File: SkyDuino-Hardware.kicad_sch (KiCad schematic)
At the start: 44 parts, among them J1 PWR, J10 AUX2, J2 BT, J3 ET, J4 Drum, J5 Filter, J6 Exhaust, J7 Cooling, J8 NTC, J9 AUX1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

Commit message: Add Quick Connect Tabs and footprints
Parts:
- ACL1, ACN1, HEAT1, HEAT2: value Spade Conn -> QC 19705-4303; footprint (none) -> Connectors:QuickConnect_Tab_Molex_19705-4303; Mouser pn (none) -> 538-19705-4303
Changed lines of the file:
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@@
 	)
 	(symbol
+		(lib_id "Connector_Generic:Conn_01x01")
+		(at 27.94 181.61 180)
+		(unit 1)
+		(exclude_from_sim no)
+		(in_bom yes)
+		(on_board yes)
+		(dnp no)
+		(property "Reference" "ACN1"
+			(at 22.86 181.61 0)
+			(effects
+				(font
+					(size 1.27 1.27)
+				)
+			)
+		)
+		(property "Value" "QC 19705-4303"
+			(at 27.94 177.8 0)
+			(effects
+				(font
+					(size 1.27 1.27)
+				)
+				(hide yes)
+			)
+		)
+		(property "Footprint" "Connectors:QuickConnect_Tab_Molex_19705-4303"
+			(at 27.94 181.61 0)
+			(effects
+				(font
+					(size 1.27 1.27)
+				)
+				(hide yes)
+			)
+		)
+		(property "Datasheet" "https://www.molex.com/content/dam/molex/molex-dot-com/products/automated/en-us/salesdrawingpdf/197/19705/197054303_sd.pdf"
+			(at 27.94 181.61 0)
+			(effects
+				(font
+					(size 1.27 1.27)
+				)
+				(hide yes)
+			)
+		)
+		(property "Description" "Terminals QUICK DISCONNECT TAB"
+			(at 27.94 181.61 0)
+			(effects
+				(font
+					(size 1.27 1.27)
+				)
+				(hide yes)
+			)
+		)
+		(property "Mouser pn" "538-19705-4303"
+			(at 27.94 181.61 0)
+			(effects
+				(font
+					(size 1.27 1.27)
+				)
+				(hide yes)
+			)
+		)
+		(pin "1"
+		)
+		(instances
+			(project "SkyDuino-Hardware"
+				(path "/a6671232-96de-4e23-ad68-f9378c1c0159"
+					(reference "ACN1")
+					(unit 1)
+				)
+			)
+		)
+	)
+	(symbol
 		(lib_id "power:GND")
 		(at 110.49 52.07 0)
@@
 			)
 		)
-		(property "Value" "Spade Conn"
+		(property "Value" "QC 19705-4303"
 			(at 27.94 172.72 0)
 			(effects
@@
 			)
 		)
-		(property "Footprint" ""
+		(property "Footprint" "Connectors:QuickConnect_Tab_Molex_19705-4303"
 			(at 27.94 176.53 0)
 			(effects
@@
 			)
 		)
-		(property "Datasheet" "~"
+		(property "Datasheet" "https://www.molex.com/content/dam/molex/molex-dot-com/products/automated/en-us/salesdrawingpdf/197/19705/197054303_sd.pdf"
 			(at 27.94 176.53 0)
 			(effects
@@
 			)
 		)
-		(property "Description" ""
+		(property "Description" "Terminals QUICK DISCONNECT TAB"
+			(at 27.94 176.53 0)
+			(effects
+				(font
+					(size 1.27 1.27)
+				)
+				(hide yes)
+			)
+		)
+		(property "Mouser pn" "538-19705-4303"
 			(at 27.94 176.53 0)
 			(effects
@@
 			)
 		)
-		(property "Value" "Spade Conn"
+		(property "Value" "QC 19705-4303"
 			(at 27.94 167.64 0)
 			(effects
@@
 			)
 		)
-		(property "Footprint" ""
+		(property "Footprint" "Connectors:QuickConnect_Tab_Molex_19705-4303"
 			(at 27.94 171.45 0)
 			(effects
@@
 			)
 		)
-		(property "Datasheet" "~"
+		(property "Datasheet" "https://www.molex.com/content/dam/molex/molex-dot-com/products/automated/en-us/salesdrawingpdf/197/19705/197054303_sd.pdf"
+			(at 27.94 171.45 0)
+			(effects
+				(font
+					(size 1.27 1.27)
+				)
+				(hide yes)
+			)
+		)
+		(property "Description" "Terminals QUICK DISCONNECT TAB"
 			(at 27.94 171.45 0)
 			(effects
@@
 			)
 		)
-		(property "Description" ""
+		(property "Mouser pn" "538-19705-4303"
 			(at 27.94 171.45 0)
 			(effects
@@
 	)
 	(symbol
-		(lib_id "Connector_Generic:Conn_01x01")
-		(at 27.94 186.69 180)
-		(unit 1)
-		(exclude_from_sim no)
-		(in_bom yes)
-		(on_board yes)
-		(dnp no)
-		(property "Reference" "HEAT2"
-			(at 22.86 186.69 0)
-			(effects
-				(font
-					(size 1.27 1.27)
-				)
-			)
-		)
-		(property "Value" "Spade Conn"
-			(at 20.32 186.69 0)
-			(effects
-				(font
-					(size 1.27 1.27)
-				)
-				(hide yes)
-			)
-		)
-		(property "Footprint" ""
-			(at 27.94 186.69 0)
-			(effects
-				(font
-					(size 1.27 1.27)
-				)
-				(hide yes)
-			)
-		)
-		(property "Datasheet" "~"
-			(at 27.94 186.69 0)
-			(effects
-				(font
-					(size 1.27 1.27)
-				)
-				(hide yes)
-			)
-		)
-		(property "Description" ""
-			(at 27.94 186.69 0)
-			(effects
-				(font
-					(size 1.27 1.27)
-				)
-				(hide yes)
-			)
-		)
-		(pin "1"
-		)
-		(instances
-			(project "SkyDuino-Hardware"
-				(path "/a6671232-96de-4e23-ad68-f9378c1c0159"
-					(reference "HEAT2")
-					(unit 1)
-				)
-			)
-		)
-	)
-	(symbol
 		(lib_id "Device:C")
 		(at 110.49 41.91 0)
@@
 	)
 	(symbol
-		(lib_id "Connector_Generic:Conn_01x01")
-		(at 27.94 181.61 180)
-		(unit 1)
-		(exclude_from_sim no)
-		(in_bom yes)
-		(on_board yes)
-		(dnp no)
-		(property "Reference" "ACN1"
-			(at 22.86 181.61 0)
-			(effects
-				(font
-					(size 1.27 1.27)
-				)
-			)
-		)
-		(property "Value" "Spade Conn"
-			(at 27.94 177.8 0)
-			(effects
-				(font
-					(size 1.27 1.27)
-				)
-				(hide yes)
-			)
-		)
-		(property "Footprint" ""
-			(at 27.94 181.61 0)
-			(effects
-				(font
-					(size 1.27 1.27)
-				)
-				(hide yes)
-			)
-		)
-		(property "Datasheet" "~"
-			(at 27.94 181.61 0)
-			(effects
-				(font
-					(size 1.27 1.27)
-				)
-				(hide yes)
-			)
-		)
-		(property "Description" ""
-			(at 27.94 181.61 0)
-			(effects
-				(font
-					(size 1.27 1.27)
-				)
-				(hide yes)
-			)
-		)
-		(pin "1"
-		)
-		(instances
-			(project "SkyDuino-Hardware"
-				(path "/a6671232-96de-4e23-ad68-f9378c1c0159"
-					(reference "ACN1")
-					(unit 1)
-				)
-			)
-		)
-	)
-	(symbol
 		(lib_id "Device:C_Polarized_Small")
 		(at 121.92 41.91 0)
@@
 					(unit 1)
 				)
+			)
+		)
+	)
+	(symbol
+		(lib_id "Connector_Generic:Conn_01x01")
+		(at 27.94 186.69 180)
+		(unit 1)
+		(exclude_from_sim no)
+		(in_bom yes)
+		(on_board yes)
+		(dnp no)
+		(property "Reference" "HEAT2"
+			(at 22.86 186.69 0)
+			(effects
+				(font
+					(size 1.27 1.27)
+				)
+			)
+		)
+		(property "Value" "QC 19705-4303"
+			(at 27.94 182.88 0)
+			(effects
+				(font
+					(size 1.27 1.27)
+				)
+				(hide yes)
+			)
+		)
+		(property "Footprint" "Connectors:QuickConnect_Tab_Molex_19705-4303"
+			(at 27.94 186.69 0)
+			(effects
+				(font
+					(size 1.27 1.27)
+				)
+				(hide yes)
+			)
+		)
+		(property "Datasheet" "https://www.molex.com/content/dam/molex/molex-dot-com/products/automated/en-us/salesdrawingpdf/197/19705/197054303_sd.pdf"
+			(at 27.94 186.69 0)
+			(effects
+				(font
+					(size 1.27 1.27)
+				)
+				(hide yes)
+			)
+		)
+		(property "Description" "Terminals QUICK DISCONNECT TAB"
+			(at 27.94 186.69 0)
+			(effects
+				(font
+					(size 1.27 1.27)
+				)
+				(hide yes)
+			)
+		)
+		(property "Mouser pn" "538-19705-4303"
+			(at 27.94 186.69 0)
+			(effects
+				(font
+					(size 1.27 1.27)
+				)
+				(hide yes)
+			)
+		)
+		(pin "1"
+		)
+		(instances
+			(project "SkyDuino-Hardware"
+				(path "/a6671232-96de-4e23-ad68-f9378c1c0159"
+					(reference "HEAT2")
+					(unit 1)
+				)

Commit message: Update footprints
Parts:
- J2, J3: footprint Connector_SH:KF7.62_2P -> Connectors:KF7.62_2P
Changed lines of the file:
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@@
 			)
 		)
-		(property "Footprint" "Connector_SH:KF7.62_2P"
+		(property "Footprint" "Connectors:KF7.62_2P"
 			(at 212.09 76.2 0)
 			(effects
@@
 			)
 		)
-		(property "Footprint" "Connector_SH:KF7.62_2P"
+		(property "Footprint" "Connectors:KF7.62_2P"
 			(at 212.09 38.1 0)
 			(effects

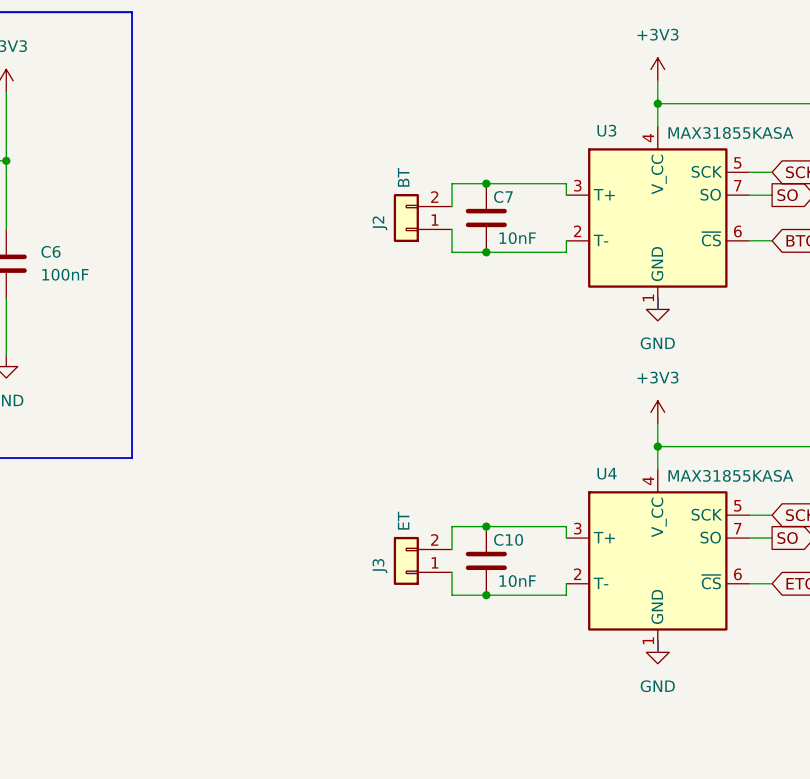
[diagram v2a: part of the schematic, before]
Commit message: Optimize pinouts
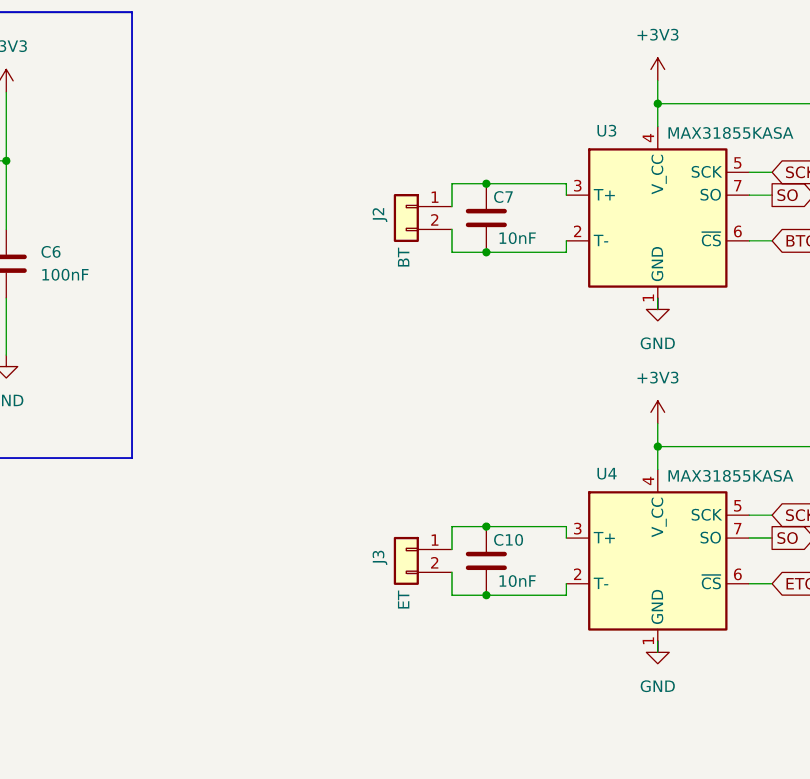
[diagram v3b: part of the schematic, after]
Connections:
- net at C10.1, U4.3 (T+): now also J3.1 (Pin_1); no longer J3.2 (Pin_2)
- net at C10.2, U4.2 (T-): now also J3.2 (Pin_2); no longer J3.1 (Pin_1)
- net at C7.1, U3.3 (T+): now also J2.1 (Pin_1); no longer J2.2 (Pin_2)
- net at C7.2, U3.2 (T-): now also J2.2 (Pin_2); no longer J2.1 (Pin_1)
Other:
- moved on the sheet: J2, J3
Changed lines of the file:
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@@
 	(symbol
 		(lib_id "Connector_Generic:Conn_01x02")
-		(at 212.09 76.2 180)
+		(at 212.09 73.66 0)
+		(mirror y)
 		(unit 1)
 		(exclude_from_sim no)
@@
 		(dnp no)
 		(property "Reference" "J3"
-			(at 209.042 76.2 90)
+			(at 209.042 73.66 90)
 			(effects
 				(font
@@
 		)
 		(property "Value" "ET"
-			(at 211.836 71.628 90)
+			(at 211.836 78.232 90)
 			(effects
 				(font
@@
 		)
 		(property "Footprint" "Connectors:KF7.62_2P"
-			(at 212.09 76.2 0)
+			(at 212.09 73.66 0)
 			(effects
 				(font
@@
 		)
 		(property "Datasheet" "~"
-			(at 212.09 76.2 0)
+			(at 212.09 73.66 0)
 			(effects
 				(font
@@
 		)
 		(property "Description" "Generic connector, single row, 01x02, script generated (kicad-library-utils/schlib/autogen/connector/)"
-			(at 212.09 76.2 0)
+			(at 212.09 73.66 0)
 			(effects
 				(font
@@
 	(symbol
 		(lib_id "Connector_Generic:Conn_01x02")
-		(at 212.09 38.1 180)
+		(at 212.09 35.56 0)
+		(mirror y)
 		(unit 1)
 		(exclude_from_sim no)
@@
 		(dnp no)
 		(property "Reference" "J2"
-			(at 209.042 38.1 90)
+			(at 209.042 35.56 90)
 			(effects
 				(font
@@
 		)
 		(property "Value" "BT"
-			(at 211.836 33.528 90)
+			(at 211.836 40.132 90)
 			(effects
 				(font
@@
 		)
 		(property "Footprint" "Connectors:KF7.62_2P"
-			(at 212.09 38.1 0)
+			(at 212.09 35.56 0)
 			(effects
 				(font
@@
 		)
 		(property "Datasheet" "~"
-			(at 212.09 38.1 0)
+			(at 212.09 35.56 0)
 			(effects
 				(font
@@
 		)
 		(property "Description" "Generic connector, single row, 01x02, script generated (kicad-library-utils/schlib/autogen/connector/)"
-			(at 212.09 38.1 0)
+			(at 212.09 35.56 0)
 			(effects
 				(font

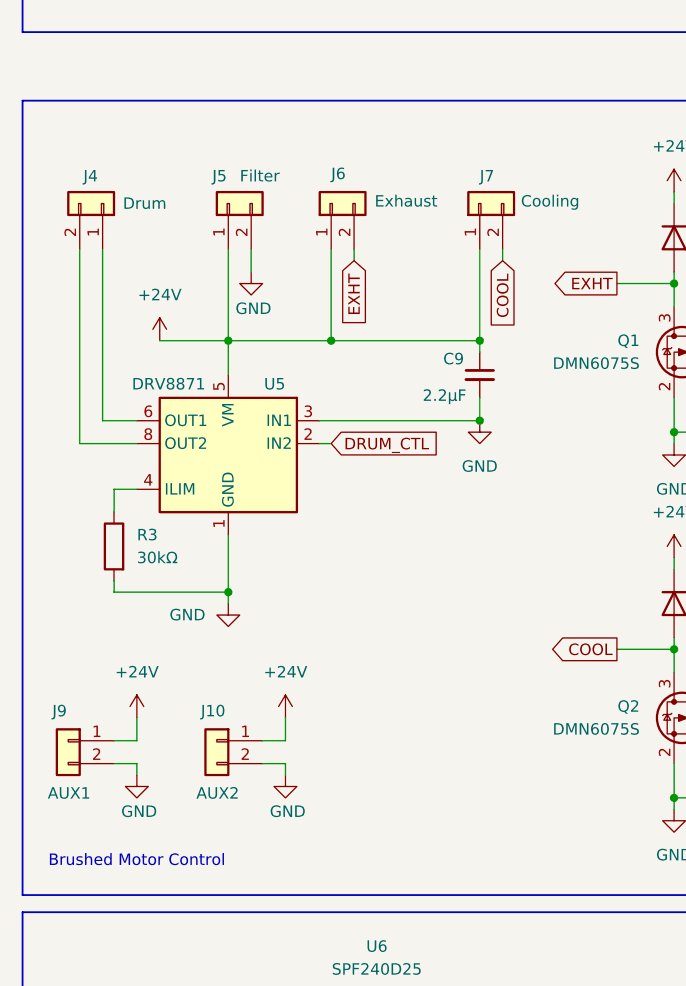
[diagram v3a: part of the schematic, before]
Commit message: Optimize pinouts
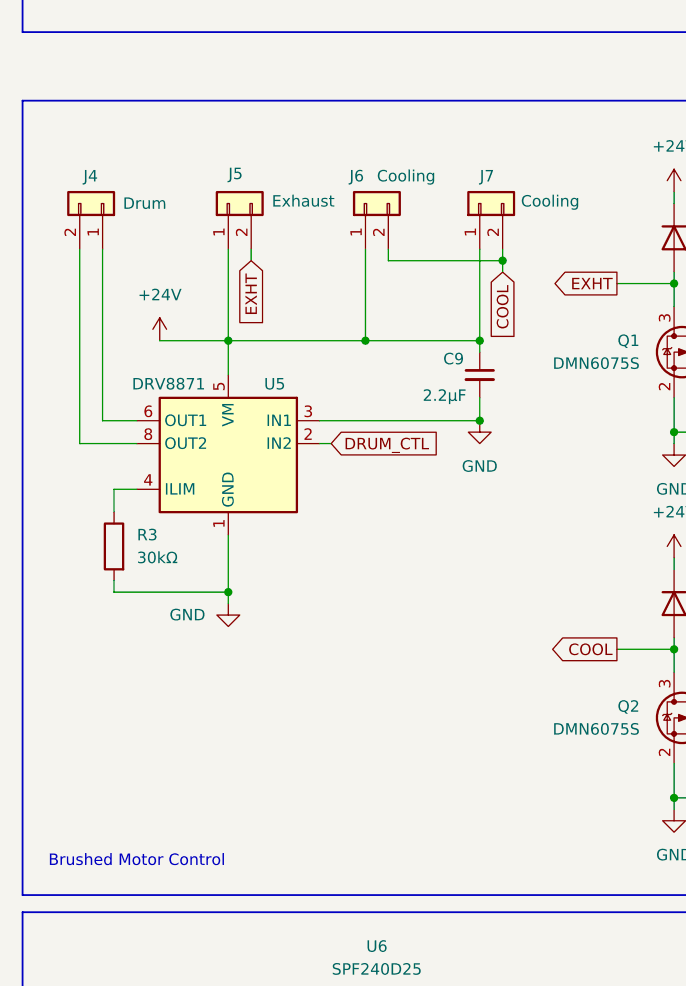
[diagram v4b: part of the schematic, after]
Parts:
- removed J10: AUX2, Connector_JST:JST_XH_B2B-XH-A_1x02_P2.50mm_Vertical, symbol Connector_Generic:Conn_01x02
- removed J9: AUX1, Connector_JST:JST_XH_B2B-XH-A_1x02_P2.50mm_Vertical, symbol Connector_Generic:Conn_01x02
- J6: renamed from J5; value Filter -> Cooling
- renumbered J6 to J5
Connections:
- net COOL: now also J6.2 (Pin_2)
- net GND: no longer J6.2 (Pin_2)
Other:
- moved on the sheet: J5, J6

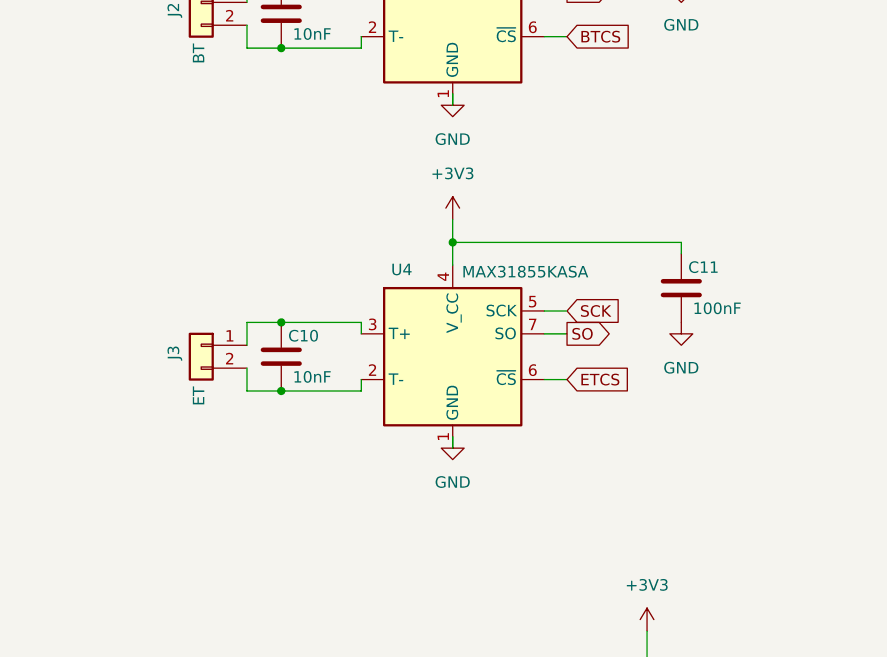
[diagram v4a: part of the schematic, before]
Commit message: Remove ET TC
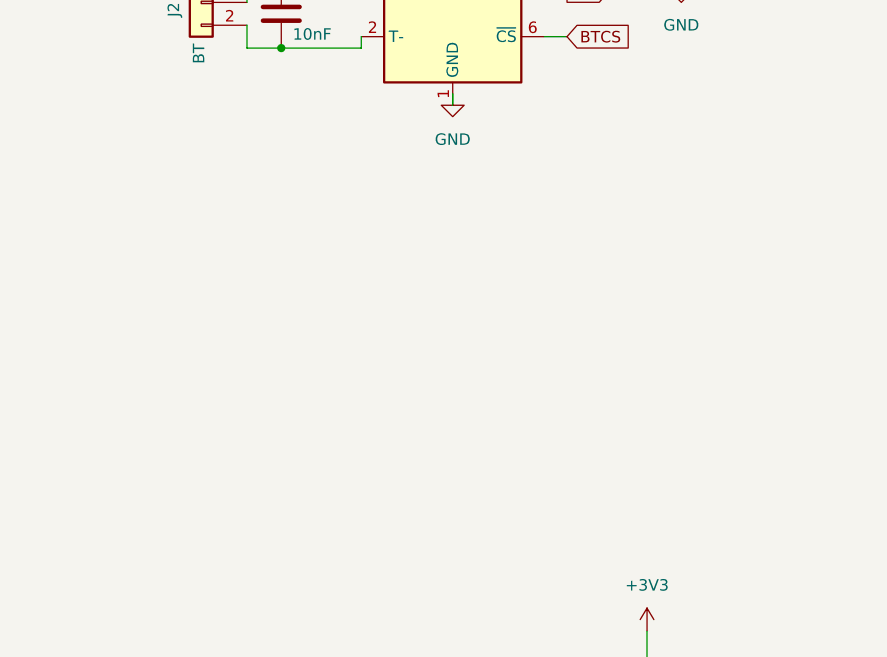
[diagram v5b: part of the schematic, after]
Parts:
- removed C10: 10nF, Capacitor_SMD:C_0805_2012Metric_Pad1.18x1.45mm_HandSolder, symbol Device:C
- removed C11: 100nF, Capacitor_SMD:C_0805_2012Metric_Pad1.18x1.45mm_HandSolder, symbol Device:C
- removed J3: ET, Connectors:KF7.62_2P, symbol Connector_Generic:Conn_01x02
- removed U4: MAX31855KASA, Package_SO:SOIC-8_3.9x4.9mm_P1.27mm, symbol Sensor_Temperature:MAX31855KASA

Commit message: Optimize pinouts, update 2.2uF caps
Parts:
- C2, C9: footprint Capacitor_SMD:C_1210_3225Metric_Pad1.33x2.70mm_HandSolder -> Capacitor_SMD:C_0805_2012Metric_Pad1.18x1.45mm_HandSolder; Mouser pn 963-HMK325B7225KM-P -> 187-CL21B225KPFNNNF
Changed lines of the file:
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@@
 			)
 		)
-		(property "Footprint" "Capacitor_SMD:C_1210_3225Metric_Pad1.33x2.70mm_HandSolder"
+		(property "Footprint" "Capacitor_SMD:C_0805_2012Metric_Pad1.18x1.45mm_HandSolder"
 			(at 52.07 30.48 0)
 			(effects
@@
 			)
 		)
-		(property "Datasheet" "https://www.mouser.com/datasheet/2/396/mlcc02_e-1307760.pdf"
+		(property "Datasheet" "https://www.mouser.com/datasheet/2/585/MLCC-1837944.pdf"
 			(at 52.07 30.48 0)
 			(effects
@@
 			)
 		)
-		(property "Description" "Unpolarized capacitor, small symbol"
+		(property "Description" "100V 2.2uF X7R 1210 10 %"
 			(at 52.07 30.48 0)
 			(effects
@@
 			)
 		)
-		(property "Mouser pn" "963-HMK325B7225KM-P"
+		(property "Mouser pn" "187-CL21B225KPFNNNF"
 			(at 52.07 30.48 0)
 			(effects
@@
 			)
 		)
-		(property "Footprint" "Capacitor_SMD:C_1210_3225Metric_Pad1.33x2.70mm_HandSolder"
+		(property "Footprint" "Capacitor_SMD:C_0805_2012Metric_Pad1.18x1.45mm_HandSolder"
 			(at 64.77 101.6 0)
 			(effects
@@
 			)
 		)
-		(property "Datasheet" "https://www.mouser.com/datasheet/2/396/mlcc02_e-1307760.pdf"
+		(property "Datasheet" "https://www.mouser.com/datasheet/2/585/MLCC-1837944.pdf"
 			(at 64.77 101.6 0)
 			(effects
@@
 			)
 		)
-		(property "Mouser pn" "963-HMK325B7225KM-P"
+		(property "Mouser pn" "187-CL21B225KPFNNNF"
 			(at 64.77 101.6 0)
 			(effects

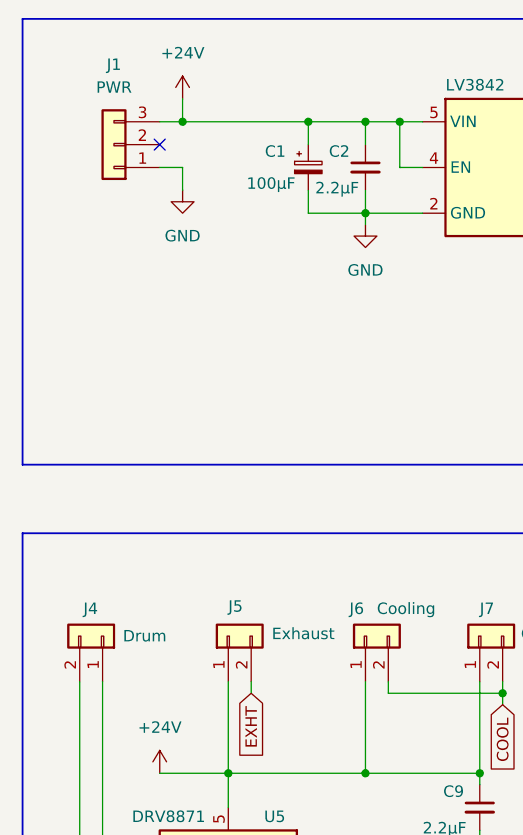
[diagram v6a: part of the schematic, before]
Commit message: Rearrange components. Fix 25MHz oscillator connection
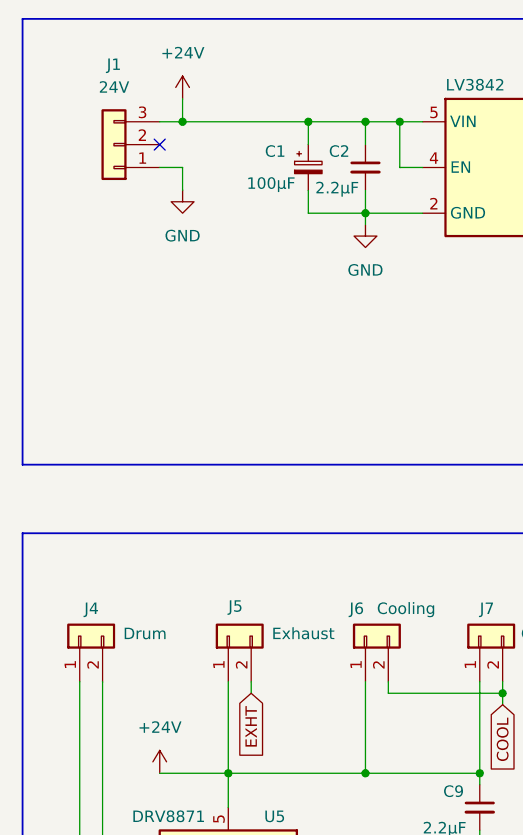
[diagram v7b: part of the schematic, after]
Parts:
- J1: value PWR -> 24V
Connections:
- net at U5.6 (OUT1): now also J4.2 (Pin_2); no longer J4.1 (Pin_1)
- net at U5.8 (OUT2): now also J4.1 (Pin_1); no longer J4.2 (Pin_2)
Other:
- moved on the sheet: J4
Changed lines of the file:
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@@
 	(symbol
 		(lib_id "Connector_Generic:Conn_01x02")
-		(at 22.86 82.55 270)
-		(mirror x)
+		(at 20.32 82.55 90)
 		(unit 1)
 		(exclude_from_sim no)
@@
 		(dnp no)
 		(property "Reference" "J4"
-			(at 22.352 79.502 90)
+			(at 20.828 79.502 90)
 			(effects
 				(font
@@
 		)
 		(property "Value" "Drum"
-			(at 29.972 82.55 90)
+			(at 25.146 82.296 90)
 			(effects
 				(font
@@
 		)
 		(property "Footprint" "Connector_JST:JST_XH_B2B-XH-A_1x02_P2.50mm_Vertical"
-			(at 22.86 82.55 0)
+			(at 20.32 82.55 0)
 			(effects
 				(font
@@
 		)
 		(property "Datasheet" "~"
-			(at 22.86 82.55 0)
+			(at 20.32 82.55 0)
 			(effects
 				(font
@@
 		)
 		(property "Description" "Generic connector, single row, 01x02, script generated (kicad-library-utils/schlib/autogen/connector/)"
-			(at 22.86 82.55 0)
+			(at 20.32 82.55 0)
 			(effects
 				(font
@@
 			)
 		)
-		(property "Value" "PWR"
+		(property "Value" "24V"
 			(at 24.13 21.59 0)
 			(effects
